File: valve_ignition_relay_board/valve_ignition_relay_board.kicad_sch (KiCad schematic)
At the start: 27 parts, among them J1 Programming Header, J5 CAN Connector Left, J6 CAN Connector Right, U1 PIC18F26K83, U2 MCP2562, U9 MCP23008-xSO, Y1 12 MHz

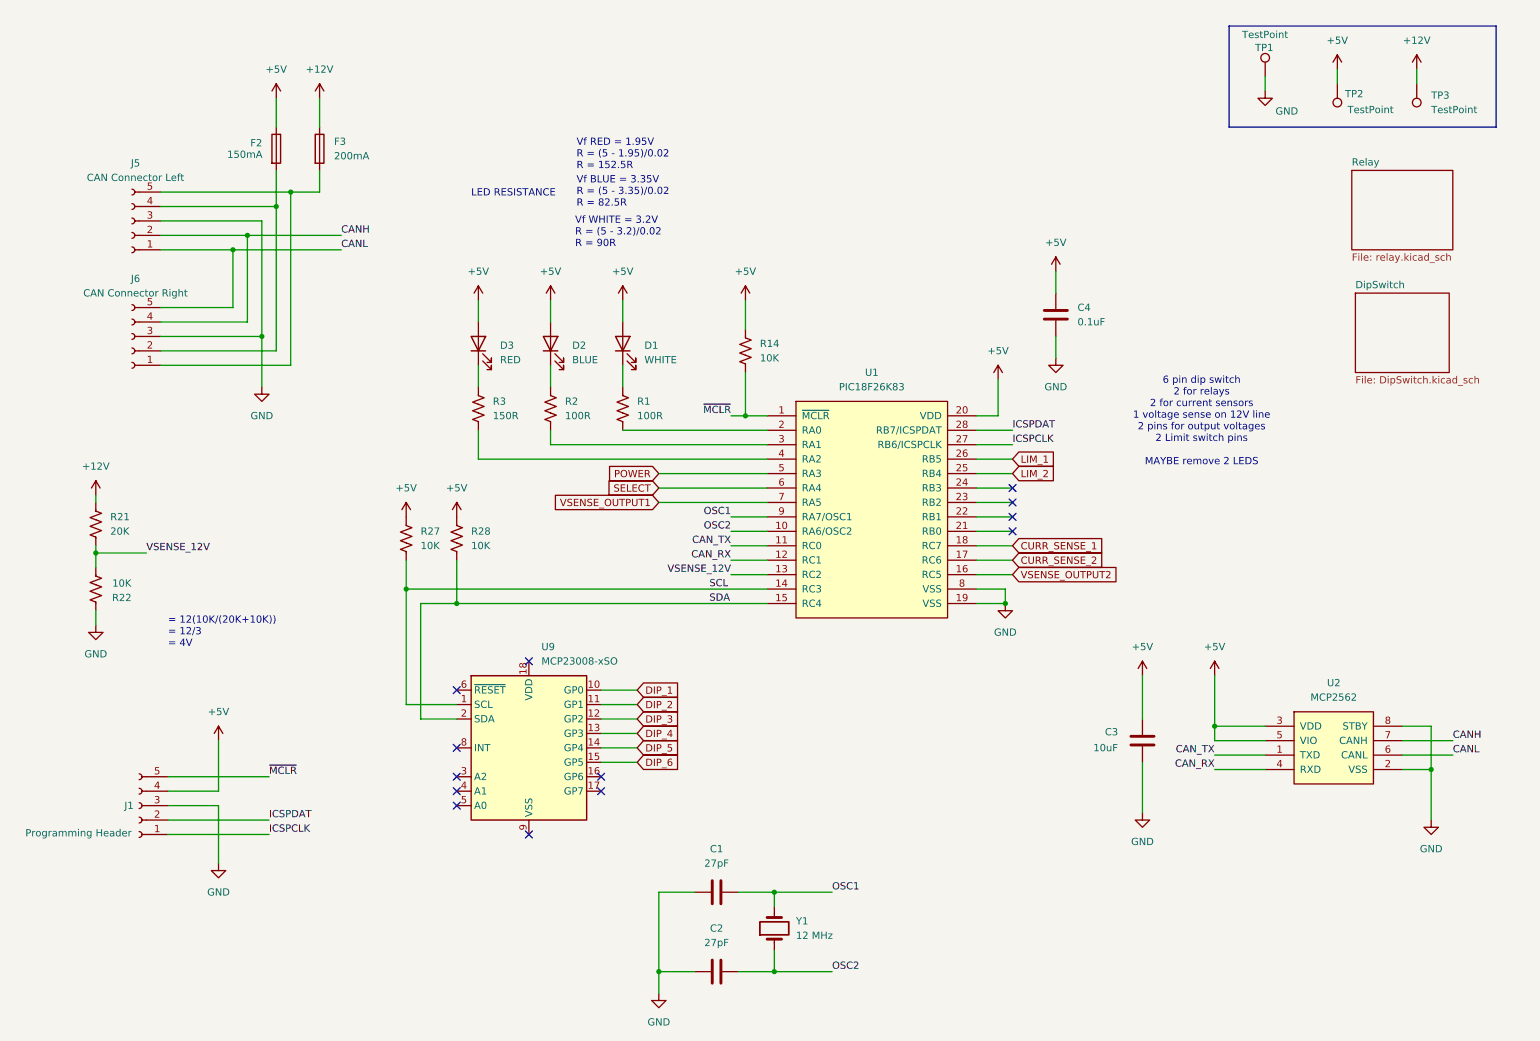
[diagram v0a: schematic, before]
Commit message: Added 4 new signals to the microcontroller
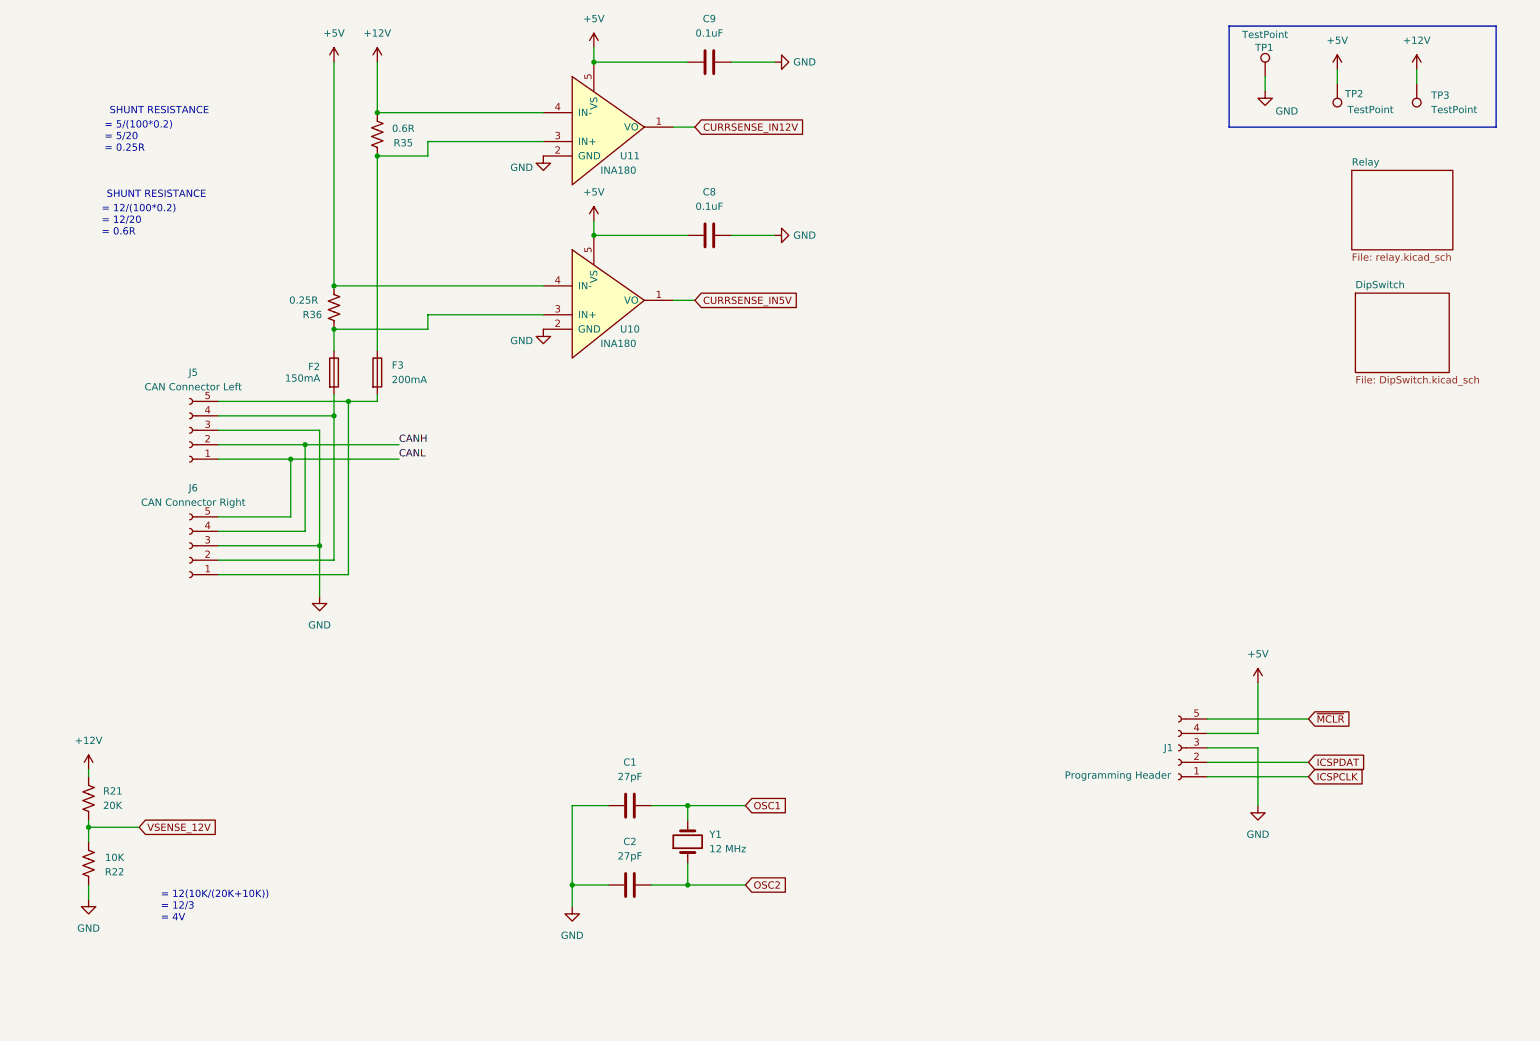
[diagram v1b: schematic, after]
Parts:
- removed C3: 10uF, Capacitor_SMD:C_0805_2012Metric_Pad1.18x1.45mm_HandSolder, symbol Device:C
- removed C4: 0.1uF, Capacitor_SMD:C_0805_2012Metric_Pad1.18x1.45mm_HandSolder, symbol Device:C
- removed D1: WHITE, LED_SMD:LED_1206_3216Metric_Pad1.42x1.75mm_HandSolder, symbol Device:LED
- removed D2: BLUE, LED_SMD:LED_1206_3216Metric_Pad1.42x1.75mm_HandSolder, symbol Device:LED
- removed D3: RED, LED_SMD:LED_1206_3216Metric_Pad1.42x1.75mm_HandSolder, symbol Device:LED
- removed R1, R2: 100R, Resistor_SMD:R_0805_2012Metric_Pad1.20x1.40mm_HandSolder, symbol Device:R_US
- removed R14, R27, R28: 10K, Resistor_SMD:R_0805_2012Metric_Pad1.20x1.40mm_HandSolder, symbol Device:R_US
- removed R3: 150R, Resistor_SMD:R_0805_2012Metric_Pad1.20x1.40mm_HandSolder, symbol Device:R_US
- removed U1: PIC18F26K83, Package_SO:SOIC-28W_7.5x18.7mm_P1.27mm, symbol canhw:PIC18F26K83
- removed U2: MCP2562, Package_SO:SOIC-8_3.9x4.9mm_P1.27mm, symbol canhw:MCP2562
- removed U9: MCP23008-xSO, Package_SO:SOIC-18W_7.5x11.6mm_P1.27mm, symbol Interface_Expansion:MCP23008-xSO
- added C8, C9: 0.1uF, Capacitor_SMD:C_0805_2012Metric_Pad1.18x1.45mm_HandSolder, symbol Device:C
- added R35: 0.6R, Resistor_SMD:R_0805_2012Metric_Pad1.20x1.40mm_HandSolder, symbol Device:R_US
- added R36: 0.25R, Resistor_SMD:R_0805_2012Metric_Pad1.20x1.40mm_HandSolder, symbol Device:R_US
- added U10, U11: INA180, Package_TO_SOT_SMD:SOT-23-5_HandSoldering, symbol canhw:INA180
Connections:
- net +12V: now also R35.2, U11.4 (IN-); no longer F3.1
- net +5V: now also C8.1, C9.1, R36.2, U10.4 (IN-), U10.5 (VS), U11.5 (VS); no longer F2.1
- net GND: now also C8.2, C9.2, U10.2 (GND), U11.2 (GND)
- new net: F2.1, R36.1, U10.3 (IN+)
- new net: F3.1, R35.1, U11.3 (IN+)
- new net CURRSENSE_IN12V: U11.1 (VO)
- new net CURRSENSE_IN5V: U10.1 (VO)
- no-connect marks 13 -> 0
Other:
- note added: "= 12/(100*0.2) = 12/20 = 0.6R"
- note added: "= 5/(100*0.2) = 5/20 = 0.25R"
- note added: "SHUNT RESISTANCE"
- note removed: "6 pin dip switch 2 for relays 2 for current sensors 1 voltage sense on 12V line 2 pins for output voltages 2 Limit switch pins MAYBE remove 2 LEDS"
- note removed: "LED RESISTANCE"
- note removed: "Vf BLUE = 3.35V R = (5 - 3.35)/0.02 R = 82.5R"
- note removed: "Vf RED = 1.95V R = (5 - 1.95)/0.02 R = 152.5R"
- note removed: "Vf WHITE = 3.2V R = (5 - 3.2)/0.02 R = 90R"
- moved on the sheet: C1, C2, F2, F3, J1, J5, J6, R21, R22, Y1
